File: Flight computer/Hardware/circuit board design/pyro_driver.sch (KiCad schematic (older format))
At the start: 12 parts, among them J4 Conn_01x06_Female, U1 LM2903, U5 LM2903, U6 Si7232DN

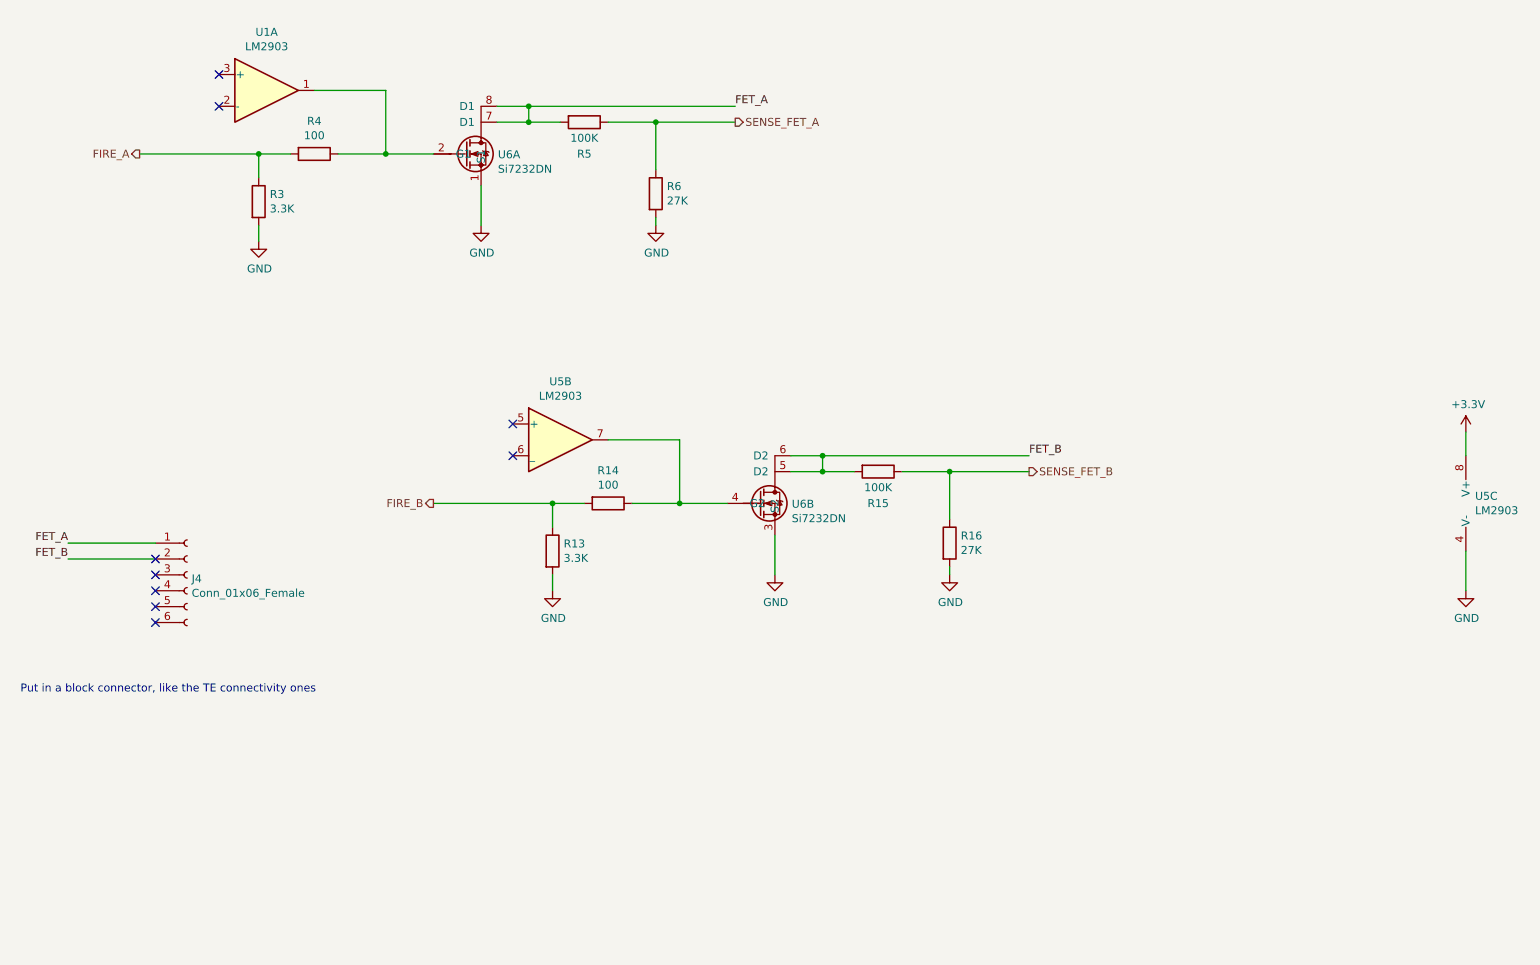
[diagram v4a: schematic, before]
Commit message: more upgrades
- removed the comparators
- added the cost and link to buy components
- added in a symbol for USB
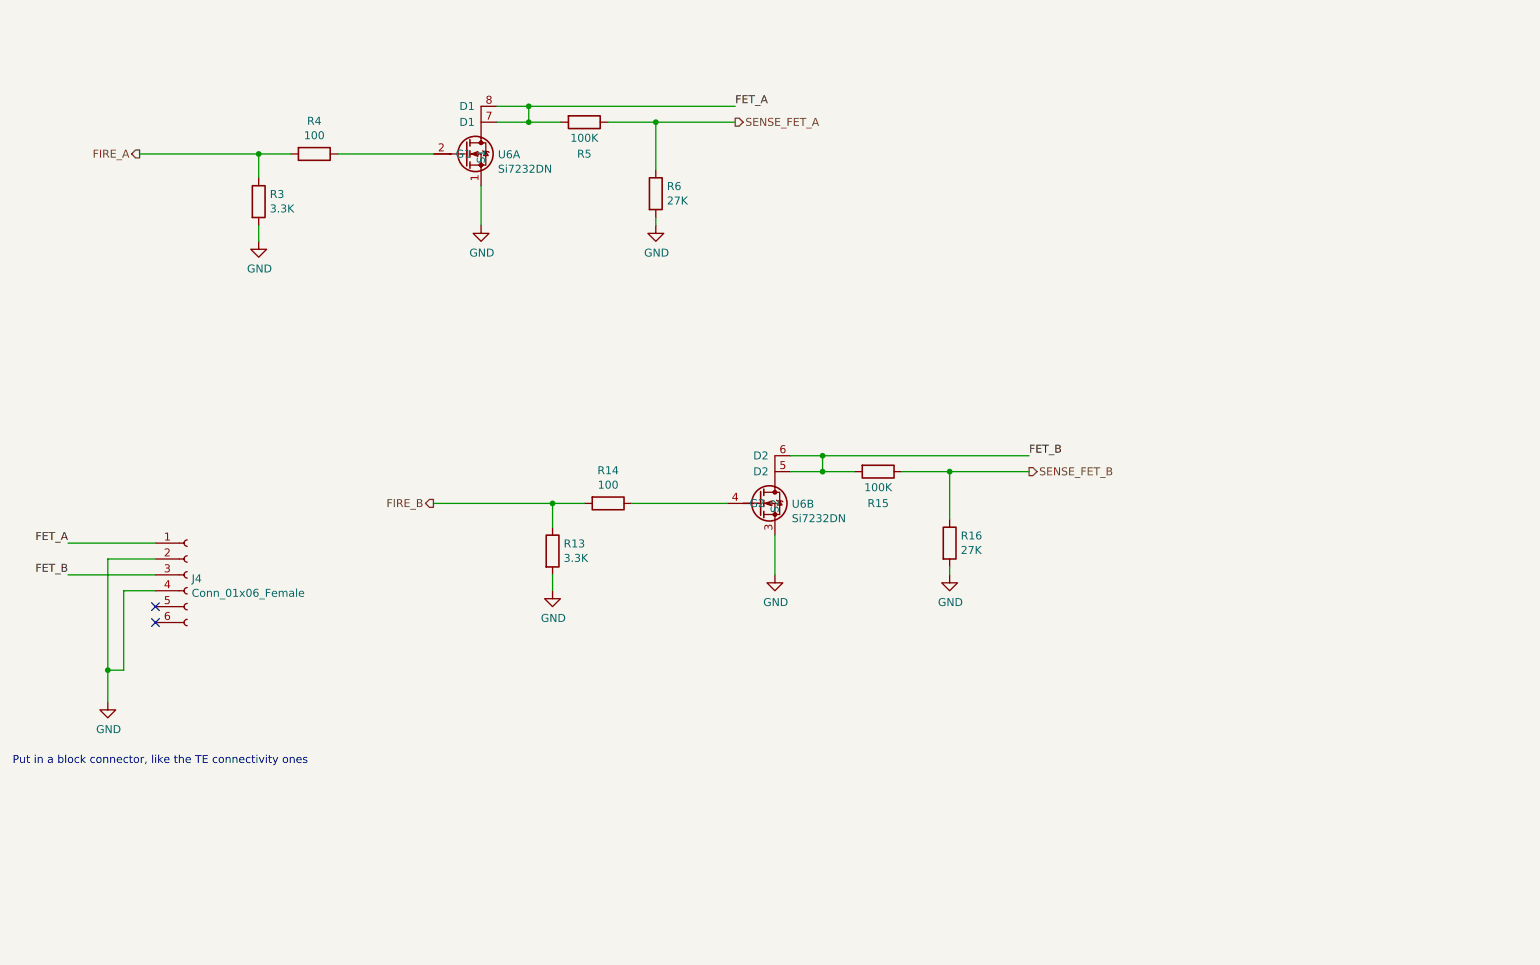
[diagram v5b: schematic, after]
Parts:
- removed U1, U5: LM2903, symbol Comparator:LM2903
- U6: Purchase link (none) -> https://www.mouser.co.uk/ProductDetail/Vishay-Siliconix/SI7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
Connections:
- net FET_B: now also J4.3 (Pin_3); no longer J4.2 (Pin_2)
- net GND: now also J4.2 (Pin_2), J4.4 (Pin_4)
- no-connect marks 9 -> 2
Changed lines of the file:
@@
 $EndDescr
-$Comp
-L Comparator:LM2903 U1
-U 1 1 5D6C6230
-P 2600 1050
-F 0 "U1" H 2600 1417 50  0000 C CNN
-F 1 "LM2903" H 2600 1326 50  0000 C CNN
-F 2 "" H 2600 1050 50  0001 C CNN
-F 3 "http://www.ti.com/lit/ds/symlink/lm393-n.pdf" H 2600 1050 50  0001 C CNN
-	1    2600 1050
-	1    0    0    -1
-$EndComp
 $Comp
 L circuit-board-design-rescue:Si7232DN-Driver_FET U6
@@
 F 2 "Package_SO:Vishay_PowerPAK_1212-8_Dual" H 3800 1250 50  0001 C CNN
 F 3 "https://www.vishay.com/docs/68986/si7232dn.pdf" H 3950 1000 50  0001 C CNN
+F 4 "https://www.mouser.co.uk/ProductDetail/Vishay-Siliconix/SI7232DN-T1-GE3?qs=%252BPu8jn5UVnH5FJ8Jo4EbFw%3D%3D" H 3950 1000 50  0001 C CNN "Purchase link"
 	1    3950 1000
 	1    0    0    -1
@@
 FET_A
 Wire Wire Line
-	2900 1050 3350 1050
-Wire Wire Line
-	3350 1050 3350 1450
-Wire Wire Line
-	3350 1450 3650 1450
-Wire Wire Line
-	3350 1450 3050 1450
-Connection ~ 3350 1450
-Wire Wire Line
 	2550 1450 2550 1600
 Connection ~ 2550 1450
@@
 Text HLabel 1800 1450 0    50   Output ~ 0
 FIRE_A
-$Comp
-L power:GND #PWR027
-U 1 1 5D6B2880
-P 10150 4200
-F 0 "#PWR027" H 10150 3950 50  0001 C CNN
-F 1 "GND" H 10155 4027 50  0000 C CNN
-F 2 "" H 10150 4200 50  0001 C CNN
-F 3 "" H 10150 4200 50  0001 C CNN
-	1    10150 4200
-	1    0    0    -1
-$EndComp
-Wire Wire Line
-	10150 3950 10150 4200
-$Comp
-L power:+3.3V #PWR026
-U 1 1 5D6B231C
-P 10150 3200
-F 0 "#PWR026" H 10150 3050 50  0001 C CNN
-F 1 "+3.3V" H 10165 3373 50  0000 C CNN
-F 2 "" H 10150 3200 50  0001 C CNN
-F 3 "" H 10150 3200 50  0001 C CNN
-	1    10150 3200
-	1    0    0    -1
-$EndComp
-$Comp
-L Comparator:LM2903 U5
-U 3 1 5D6B191C
-P 10250 3650
-F 0 "U5" H 10208 3696 50  0000 L CNN
-F 1 "LM2903" H 10208 3605 50  0000 L CNN
-F 2 "" H 10250 3650 50  0001 C CNN
-F 3 "http://www.ti.com/lit/ds/symlink/lm393-n.pdf" H 10250 3650 50  0001 C CNN
-	3    10250 3650
-	1    0    0    -1
-$EndComp
-Wire Wire Line
-	10150 3350 10150 3200
-Text Notes 1050 4850 0    50   ~ 0
+Text Notes 1000 5300 0    50   ~ 0
 Put in a block connector, like the TE connectivity ones\n
 $Comp
@@
 	1    0    0    -1
 $EndComp
-NoConn ~ 2300 1150
-NoConn ~ 2300 950
-NoConn ~ 1900 4000
-NoConn ~ 1900 4100
-NoConn ~ 1900 4200
 NoConn ~ 1900 4300
 NoConn ~ 1900 4400
@@
 Wire Wire Line
 	1350 3900 1900 3900
-$Comp
-L Comparator:LM2903 U5
-U 2 1 5D743B77
-P 4450 3250
-F 0 "U5" H 4450 3617 50  0000 C CNN
-F 1 "LM2903" H 4450 3526 50  0000 C CNN
-F 2 "" H 4450 3250 50  0001 C CNN
-F 3 "http://www.ti.com/lit/ds/symlink/lm393-n.pdf" H 4450 3250 50  0001 C CNN
-	2    4450 3250
-	1    0    0    -1
-$EndComp
 $Comp
 L circuit-board-design-rescue:Si7232DN-Driver_FET U?
@@
 F 2 "Package_SO:Vishay_PowerPAK_1212-8_Dual" H 5650 3450 50  0001 C CNN
 F 3 "https://www.vishay.com/docs/68986/si7232dn.pdf" H 5800 3200 50  0001 C CNN
+F 4 "https://www.mouser.co.uk/ProductDetail/Vishay-Siliconix/SI7232DN-T1-GE3?qs=%252BPu8jn5UVnH5FJ8Jo4EbFw%3D%3D" H 5800 3200 50  0001 C CNN "Purchase link"
 	2    5800 3200
 	1    0    0    -1
@@
 FET_B
 Wire Wire Line
-	4750 3250 5200 3250
-Wire Wire Line
-	5200 3250 5200 3650
-Wire Wire Line
-	5200 3650 5500 3650
-Wire Wire Line
-	5200 3650 4900 3650
-Connection ~ 5200 3650
-Wire Wire Line
 	4400 3650 4400 3800
 Connection ~ 4400 3650
@@
 Text HLabel 3650 3650 0    50   Output ~ 0
 FIRE_B
-NoConn ~ 4150 3350
-NoConn ~ 4150 3150
-Text Label 1350 4000 2    50   ~ 0
+Text Label 1350 4100 2    50   ~ 0
 FET_B
 Wire Wire Line
-	1350 4000 1900 4000
+	1350 4100 1900 4100
 Wire Wire Line
 	5800 4100 5800 3850
+$Comp
+L power:GND #PWR045
+U 1 1 5D70E267
+P 1600 4900
+F 0 "#PWR045" H 1600 4650 50  0001 C CNN
+F 1 "GND" H 1605 4727 50  0000 C CNN
+F 2 "" H 1600 4900 50  0001 C CNN
+F 3 "" H 1600 4900 50  0001 C CNN
+	1    1600 4900
+	1    0    0    -1
+$EndComp
+Wire Wire Line
+	1900 4000 1600 4000
+Wire Wire Line
+	1600 4000 1600 4700
+Wire Wire Line
+	1900 4200 1700 4200
+Wire Wire Line
+	1700 4700 1600 4700
+Wire Wire Line
+	1700 4200 1700 4700
+Connection ~ 1600 4700
+Wire Wire Line
+	1600 4700 1600 4900
+Wire Wire Line
+	3050 1450 3650 1450
+Wire Wire Line
+	4900 3650 5500 3650
 $EndSCHEMATC

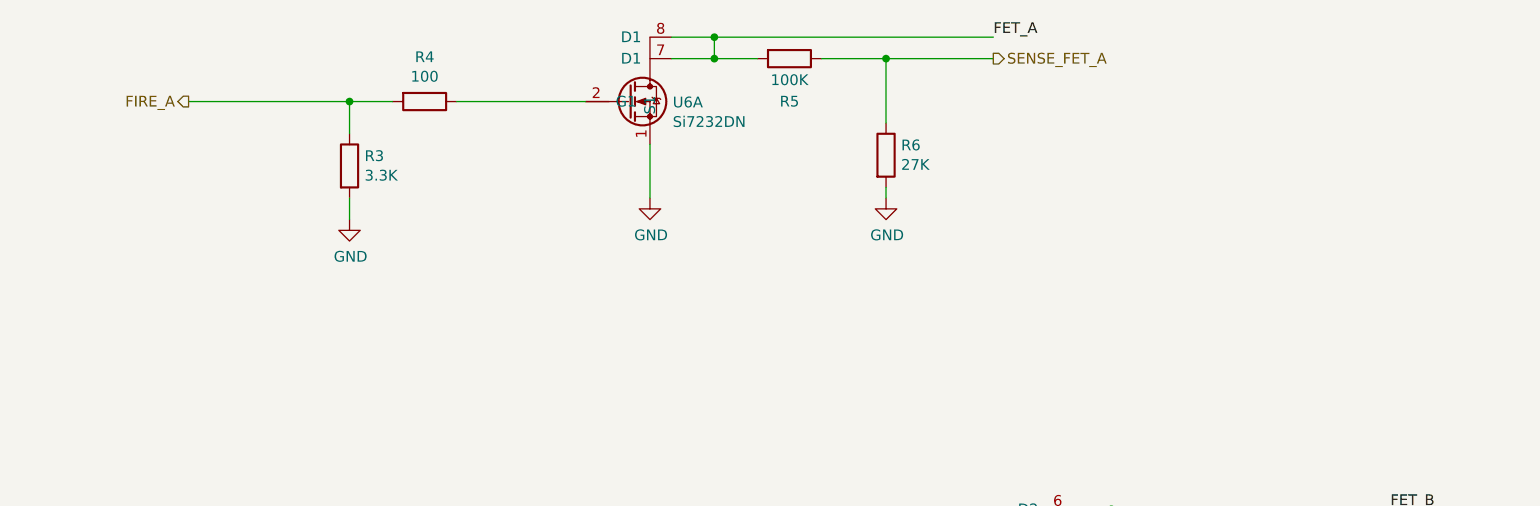
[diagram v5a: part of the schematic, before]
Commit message: put in the IIS2MDC magnetometer
-fixed the error  spi connection pins for Flash chip
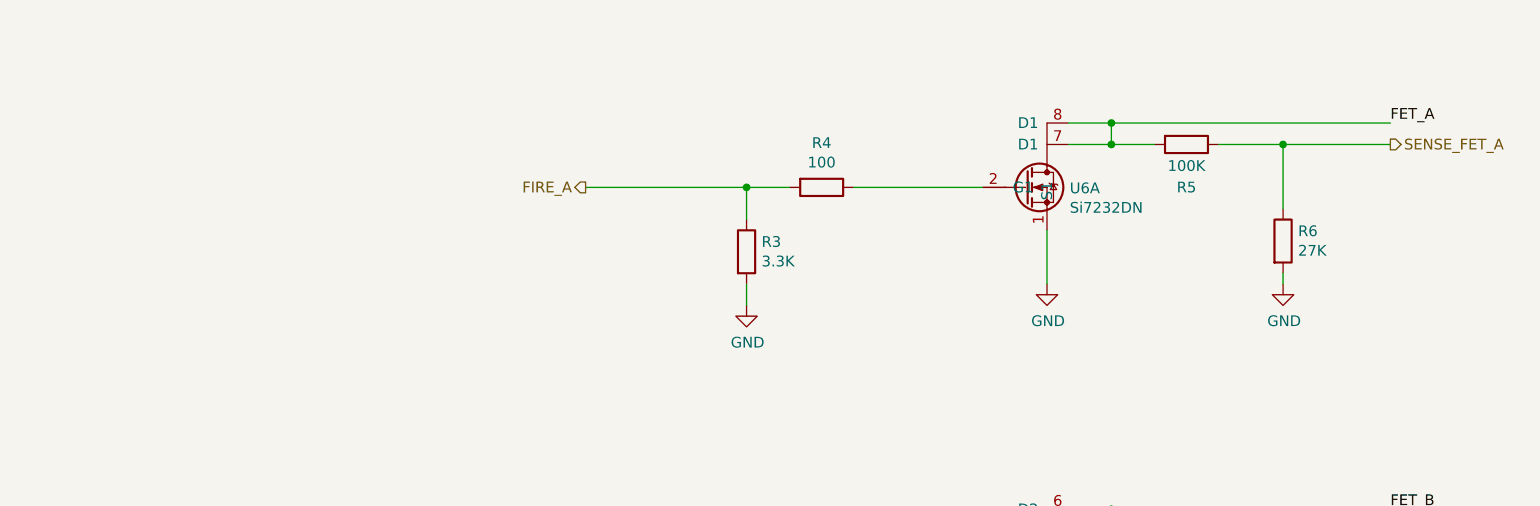
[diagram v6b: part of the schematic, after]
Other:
- moved on the sheet: R3, R4, R5, R6, U6A
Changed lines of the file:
@@
 L circuit-board-design-rescue:Si7232DN-Driver_FET U6
 U 1 1 5D696EFB
-P 3950 1000
+P 5800 1400
 AR Path="/5D696EFB" Ref="U6"  Part="1"
 AR Path="/5D6468D5/5D696EFB" Ref="U6"  Part="1"
-F 0 "U6" H 4056 546 50  0000 L CNN
-F 1 "Si7232DN" H 4056 455 50  0000 L CNN
-F 2 "Package_SO:Vishay_PowerPAK_1212-8_Dual" H 3800 1250 50  0001 C CNN
-F 3 "https://www.vishay.com/docs/68986/si7232dn.pdf" H 3950 1000 50  0001 C CNN
-F 4 "https://www.mouser.co.uk/ProductDetail/Vishay-Siliconix/SI7232DN-T1-GE3?qs=%252BPu8jn5UVnH5FJ8Jo4EbFw%3D%3D" H 3950 1000 50  0001 C CNN "Purchase link"
-	1    3950 1000
+F 0 "U6" H 5906 946 50  0000 L CNN
+F 1 "Si7232DN" H 5906 855 50  0000 L CNN
+F 2 "Package_SO:Vishay_PowerPAK_1212-8_Dual" H 5650 1650 50  0001 C CNN
+F 3 "https://www.vishay.com/docs/68986/si7232dn.pdf" H 5800 1400 50  0001 C CNN
+F 4 "https://www.mouser.co.uk/ProductDetail/Vishay-Siliconix/SI7232DN-T1-GE3?qs=%252BPu8jn5UVnH5FJ8Jo4EbFw%3D%3D" H 5800 1400 50  0001 C CNN "Purchase link"
+	1    5800 1400
 	1    0    0    -1
 $EndComp
@@
 L power:GND #PWR024
 U 1 1 5D69AE81
-P 3950 1900
-F 0 "#PWR024" H 3950 1650 50  0001 C CNN
-F 1 "GND" H 3955 1727 50  0000 C CNN
-F 2 "" H 3950 1900 50  0001 C CNN
-F 3 "" H 3950 1900 50  0001 C CNN
-	1    3950 1900
-	1    0    0    -1
-$EndComp
-Wire Wire Line
-	3950 1900 3950 1650
+P 5800 2300
+F 0 "#PWR024" H 5800 2050 50  0001 C CNN
+F 1 "GND" H 5805 2127 50  0000 C CNN
+F 2 "" H 5800 2300 50  0001 C CNN
+F 3 "" H 5800 2300 50  0001 C CNN
+	1    5800 2300
+	1    0    0    -1
+$EndComp
+Wire Wire Line
+	5800 2300 5800 2050
 $Comp
 L Device:R R5
 U 1 1 5D6A50BE
-P 4600 1250
-F 0 "R5" V 4800 1250 50  0000 C CNN
-F 1 "100K" V 4700 1250 50  0000 C CNN
-F 2 "Resistor_SMD:R_0603_1608Metric" V 4530 1250 50  0001 C CNN
-F 3 "~" H 4600 1250 50  0001 C CNN
-	1    4600 1250
+P 6450 1650
+F 0 "R5" V 6650 1650 50  0000 C CNN
+F 1 "100K" V 6550 1650 50  0000 C CNN
+F 2 "Resistor_SMD:R_0603_1608Metric" V 6380 1650 50  0001 C CNN
+F 3 "~" H 6450 1650 50  0001 C CNN
+	1    6450 1650
 	0    1    1    0
 $EndComp
@@
 L Device:R R6
 U 1 1 5D6A6316
-P 5050 1700
-F 0 "R6" H 5120 1746 50  0000 L CNN
-F 1 "27K" H 5120 1655 50  0000 L CNN
-F 2 "Resistor_SMD:R_0603_1608Metric" V 4980 1700 50  0001 C CNN
-F 3 "~" H 5050 1700 50  0001 C CNN
-	1    5050 1700
-	1    0    0    -1
-$EndComp
-Wire Wire Line
-	4750 1250 5050 1250
-Wire Wire Line
-	5050 1550 5050 1250
-Wire Wire Line
-	5050 1900 5050 1850
+P 6900 2100
+F 0 "R6" H 6970 2146 50  0000 L CNN
+F 1 "27K" H 6970 2055 50  0000 L CNN
+F 2 "Resistor_SMD:R_0603_1608Metric" V 6830 2100 50  0001 C CNN
+F 3 "~" H 6900 2100 50  0001 C CNN
+	1    6900 2100
+	1    0    0    -1
+$EndComp
+Wire Wire Line
+	6600 1650 6900 1650
+Wire Wire Line
+	6900 1950 6900 1650
+Wire Wire Line
+	6900 2300 6900 2250
 $Comp
 L power:GND #PWR025
 U 1 1 5D6A67BF
-P 5050 1900
-F 0 "#PWR025" H 5050 1650 50  0001 C CNN
-F 1 "GND" H 5055 1727 50  0000 C CNN
-F 2 "" H 5050 1900 50  0001 C CNN
-F 3 "" H 5050 1900 50  0001 C CNN
-	1    5050 1900
-	1    0    0    -1
-$EndComp
-Wire Wire Line
-	4050 1250 4250 1250
-Wire Wire Line
-	4050 1150 4250 1150
-Wire Wire Line
-	4250 1250 4250 1150
-Connection ~ 4250 1250
-Wire Wire Line
-	4250 1250 4450 1250
-Connection ~ 4250 1150
-Wire Wire Line
-	4250 1150 5550 1150
-Connection ~ 5050 1250
-Wire Wire Line
-	5050 1250 5550 1250
-Text HLabel 5550 1250 2    50   Output ~ 0
+P 6900 2300
+F 0 "#PWR025" H 6900 2050 50  0001 C CNN
+F 1 "GND" H 6905 2127 50  0000 C CNN
+F 2 "" H 6900 2300 50  0001 C CNN
+F 3 "" H 6900 2300 50  0001 C CNN
+	1    6900 2300
+	1    0    0    -1
+$EndComp
+Wire Wire Line
+	5900 1650 6100 1650
+Wire Wire Line
+	5900 1550 6100 1550
+Wire Wire Line
+	6100 1650 6100 1550
+Connection ~ 6100 1650
+Wire Wire Line
+	6100 1650 6300 1650
+Connection ~ 6100 1550
+Wire Wire Line
+	6100 1550 7400 1550
+Connection ~ 6900 1650
+Wire Wire Line
+	6900 1650 7400 1650
+Text HLabel 7400 1650 2    50   Output ~ 0
 SENSE_FET_A
-Text Label 5550 1150 0    50   ~ 0
+Text Label 7400 1550 0    50   ~ 0
 FET_A
 Wire Wire Line
-	2550 1450 2550 1600
-Connection ~ 2550 1450
-Wire Wire Line
-	2550 1450 1800 1450
+	4400 1850 4400 2000
+Connection ~ 4400 1850
+Wire Wire Line
+	4400 1850 3650 1850
 $Comp
 L power:GND #PWR023
 U 1 1 5D6AF664
-P 2550 2000
-F 0 "#PWR023" H 2550 1750 50  0001 C CNN
-F 1 "GND" H 2555 1827 50  0000 C CNN
-F 2 "" H 2550 2000 50  0001 C CNN
-F 3 "" H 2550 2000 50  0001 C CNN
-	1    2550 2000
+P 4400 2400
+F 0 "#PWR023" H 4400 2150 50  0001 C CNN
+F 1 "GND" H 4405 2227 50  0000 C CNN
+F 2 "" H 4400 2400 50  0001 C CNN
+F 3 "" H 4400 2400 50  0001 C CNN
+	1    4400 2400
 	1    0    0    -1
 $EndComp
@@
 L Device:R R3
 U 1 1 5D6AFE1F
-P 2550 1750
-F 0 "R3" H 2620 1796 50  0000 L CNN
-F 1 "3.3K" H 2620 1705 50  0000 L CNN
-F 2 "Resistor_SMD:R_0603_1608Metric" V 2480 1750 50  0001 C CNN
-F 3 "~" H 2550 1750 50  0001 C CNN
-	1    2550 1750
-	1    0    0    -1
-$EndComp
-Wire Wire Line
-	2550 1900 2550 2000
+P 4400 2150
+F 0 "R3" H 4470 2196 50  0000 L CNN
+F 1 "3.3K" H 4470 2105 50  0000 L CNN
+F 2 "Resistor_SMD:R_0603_1608Metric" V 4330 2150 50  0001 C CNN
+F 3 "~" H 4400 2150 50  0001 C CNN
+	1    4400 2150
+	1    0    0    -1
+$EndComp
+Wire Wire Line
+	4400 2300 4400 2400
 $Comp
 L Device:R R4
 U 1 1 5D6B06F6
-P 2900 1450
-F 0 "R4" V 2693 1450 50  0000 C CNN
-F 1 "100" V 2784 1450 50  0000 C CNN
-F 2 "Resistor_SMD:R_0603_1608Metric" V 2830 1450 50  0001 C CNN
-F 3 "~" H 2900 1450 50  0001 C CNN
-	1    2900 1450
+P 4750 1850
+F 0 "R4" V 4543 1850 50  0000 C CNN
+F 1 "100" V 4634 1850 50  0000 C CNN
+F 2 "Resistor_SMD:R_0603_1608Metric" V 4680 1850 50  0001 C CNN
+F 3 "~" H 4750 1850 50  0001 C CNN
+	1    4750 1850
 	0    1    1    0
 $EndComp
 Wire Wire Line
-	2750 1450 2550 1450
-Text HLabel 1800 1450 0    50   Output ~ 0
+	4600 1850 4400 1850
+Text HLabel 3650 1850 0    50   Output ~ 0
 FIRE_A
 Text Notes 1000 5300 0    50   ~ 0
@@
 Text Label 7400 3350 0    50   ~ 0
 FET_B
+Text Label 1350 4100 2    50   ~ 0
+FET_B
+Wire Wire Line
+	1350 4100 1900 4100
+Wire Wire Line
+	5800 4100 5800 3850
+$Comp
+L power:GND #PWR045
+U 1 1 5D70E267
+P 1600 4900
+F 0 "#PWR045" H 1600 4650 50  0001 C CNN
+F 1 "GND" H 1605 4727 50  0000 C CNN
+F 2 "" H 1600 4900 50  0001 C CNN
+F 3 "" H 1600 4900 50  0001 C CNN
+	1    1600 4900
+	1    0    0    -1
+$EndComp
+Wire Wire Line
+	1900 4000 1600 4000
+Wire Wire Line
+	1600 4000 1600 4700
+Wire Wire Line
+	1900 4200 1700 4200
+Wire Wire Line
+	1700 4700 1600 4700
+Wire Wire Line
+	1700 4200 1700 4700
+Connection ~ 1600 4700
+Wire Wire Line
+	1600 4700 1600 4900
+Wire Wire Line
+	4900 1850 5500 1850
 Wire Wire Line
 	4400 3650 4400 3800
@@
 Text HLabel 3650 3650 0    50   Output ~ 0
 FIRE_B
-Text Label 1350 4100 2    50   ~ 0
-FET_B
-Wire Wire Line
-	1350 4100 1900 4100
-Wire Wire Line
-	5800 4100 5800 3850
-$Comp
-L power:GND #PWR045
-U 1 1 5D70E267
-P 1600 4900
-F 0 "#PWR045" H 1600 4650 50  0001 C CNN
-F 1 "GND" H 1605 4727 50  0000 C CNN
-F 2 "" H 1600 4900 50  0001 C CNN
-F 3 "" H 1600 4900 50  0001 C CNN
-	1    1600 4900
-	1    0    0    -1
-$EndComp
-Wire Wire Line
-	1900 4000 1600 4000
-Wire Wire Line
-	1600 4000 1600 4700
-Wire Wire Line
-	1900 4200 1700 4200
-Wire Wire Line
-	1700 4700 1600 4700
-Wire Wire Line
-	1700 4200 1700 4700
-Connection ~ 1600 4700
-Wire Wire Line
-	1600 4700 1600 4900
-Wire Wire Line
-	3050 1450 3650 1450
 Wire Wire Line
 	4900 3650 5500 3650
